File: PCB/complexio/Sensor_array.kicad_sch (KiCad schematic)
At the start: 39 parts, among them J3 Conn_01x12_Pin, Q1 AO3400A, U10 KTIR0711S, U11 KTIR0711S, U12 KTIR0711S, U4 KTIR0711S, U5 KTIR0711S, U6 KTIR0711S, U7 KTIR0711S, U8 KTIR0711S, U9 KTIR0711S

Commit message: Sensor array finished & main schem modified
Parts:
- removed J3: Conn_01x12_Pin, Connector_PinHeader_2.54mm:PinHeader_1x12_P2.54mm_Horizontal, symbol Connector:Conn_01x12_Pin
- added C17, C19, C21, C23, C25, C27, C28, C30, C31: 100n, Capacitor_SMD:C_0402_1005Metric, symbol Device:C
- added C18, C20, C22, C24, C26, C29, C32: 1u, Capacitor_SMD:C_0402_1005Metric, symbol Device:C
- added J1: Conn_01x21_Pin, Connector_PinHeader_1.27mm:PinHeader_1x21_P1.27mm_Horizontal, symbol Connector:Conn_01x21_Pin
- added R23, R24: 47, Resistor_SMD:R_1206_3216Metric, symbol Device:R
- added R25, R26: 47k, Resistor_SMD:R_0402_1005Metric, symbol Device:R
- added R27, R30: 10k, Resistor_SMD:R_0402_1005Metric, symbol Device:R
- added U13, U14, U15, U16, U17, U18, U19: KTIR0711S, KTIR0711S:KTIR0711S, symbol KTIR0711S:KTIR0711S
- added U20: SN74LVC16T245DGGR, SN74LVC16T245DGGR:SN74LVC16T245DGGR, symbol SN74LVC16T245DGGR:SN74LVC16T245DGGR
- R12, R13, R5, R8: footprint Resistor_SMD:R_0402_1005Metric -> Resistor_SMD:R_1206_3216Metric; JLCPCB Part # C11930 -> C702856; MFR.Part # RTT02470JTH -> RCT0647RJLF; Manufacturer RALEC -> HKR(Hong Kong Resistors); Package 0402 -> 1206
- R16: value 47 -> 47k; JLCPCB Part # C11930 -> C22356233; MFR.Part # RTT02470JTH -> RCA0247KJLF; Manufacturer RALEC -> HKR(Hong Kong Resistors)
- R17, R18: value 10k -> 47; footprint Resistor_SMD:R_0402_1005Metric -> Resistor_SMD:R_1206_3216Metric; JLCPCB Part # C174175 -> C702856; MFR.Part # RCT0210KJLF -> RCT0647RJLF; Package 0402 -> 1206
- R19, R20, R21, R22: value 10k -> 47k; JLCPCB Part # C174175 -> C22356233; MFR.Part # RCT0210KJLF -> RCA0247KJLF
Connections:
- net GND: now also C17.2, C18.2, C19.2, C20.2, C21.2, C22.2, C23.2, C24.2, C25.2, C26.2, C27.2, C28.2, C29.2, C30.2, C31.2, C32.2, J1.3 (Pin_3), U13.2 (emitter), U14.2 (emitter), U15.2 (emitter), U16.2 (emitter), U17.2 (emitter), U18.2 (emitter), U19.2 (emitter), U20.1 (1DIR), U20.10 (GND), U20.15 (GND), U20.21 (GND), U20.24 (2DIR), U20.28 (GND), U20.34 (GND), U20.39 (GND), U20.4 (GND), U20.45 (GND); no longer R19.1, R22.1
- net LED_Cathode: now also U14.4 (cathode), U15.4 (cathode), U18.4 (cathode), U19.4 (cathode); no longer U12.4 (cathode)
- net OUT1: now also U20.2 (1B1)
- net OUT2: now also U20.3 (1B2)
- net OUT3: now also U20.5 (1B3); no longer R4.1, U6.3 (collector)
- net OUT4: now also U20.6 (1B4)
- net OUT5: now also R15.1, U12.3 (collector), U20.8 (1B5); no longer R17.2, R18.2
- net OUT6: now also R19.1, U14.3 (collector), U20.9 (1B6); no longer R20.2, R21.2
- net OUT7: now also U20.11 (1B7); no longer R10.1, U10.3 (collector)
- net OUT8: now also R25.1, U18.3 (collector), U20.12 (1B8); no longer R14.1, U11.3 (collector)
- net OUT9: now also R7.1, U8.3 (collector), U20.13 (2B1); no longer R15.1, U12.3 (collector)
- net at U10.1 (anode): now also R13.2; no longer R13.1
- net at U8.1 (anode): now also R8.2; no longer R8.1
- net at U4.1 (anode): now also R5.2; no longer R12.1
- net OUT10: now reaches R9.1, U9.3 (collector)
- net OUT10: now also U20.14 (2B2); no longer R20.1
- net at U6.1 (anode): now also R12.2; no longer R5.1
- net +5V: now reaches R18.1, R19.2
- net +5V: now also C10.1, C11.1, C12.1, C13.1, C14.1, C15.1, C16.1, R10.2, R11.2, R12.1, R13.1, R14.2, R15.2, R16.2, R17.1, R2.2, R20.2, R21.2, R22.2, R3.2, R4.2, R5.1, R6.2, R7.2, R8.1, R9.2, C17.1, C18.1, C19.1, C20.1, C21.1, C22.1, C23.1, C24.1, C25.1, C26.1, C27.1, C28.1, J1.1 (Pin_1), R23.1, R24.1, R25.2, R26.2, U20.18 (VCCB), U20.7 (VCCB)
- net at R21.1: now also U16.3 (collector); no longer R22.2
- net at U12.1 (anode): now also R17.2; no longer R16.1
- net LEDON renamed ledon
- net ledon: now also J1.5 (Pin_5)
- removed net VCC: C10.1, C11.1, C12.1, C13.1, C14.1, C15.1, C16.1, R10.2, R11.2, R12.2, R13.2, R14.2, R15.2, R16.2, R2.2, R3.2, R4.2, R5.2, R6.2, R7.2, R8.2, R9.2
- new net: R22.1, U17.3 (collector)
- new net: R10.1, U10.3 (collector)
- new net: R4.1, U6.3 (collector)
- new net: U16.4 (cathode), U18.1 (anode)
- new net: U12.4 (cathode), U14.1 (anode)
- new net: R23.2, U16.1 (anode)
- new net: U13.4 (cathode), U15.1 (anode)
- new net: U17.4 (cathode), U19.1 (anode)
- new net: R18.2, U13.1 (anode)
- new net: R24.2, U17.1 (anode)
- new net +3V3: C29.1, C30.1, C31.1, C32.1, J1.2 (Pin_2), R27.1, R30.1, U20.31 (VCCA), U20.42 (VCCA)
- new net OUT11: U20.16 (2B3)
- new net OUT12: R14.1, U11.3 (collector), U20.17 (2B4)
- new net OUT13: R16.1, U13.3 (collector), U20.19 (2B5)
- new net OUT14: R20.1, U15.3 (collector), U20.20 (2B6)
- new net OUT15: U20.22 (2B7)
- new net OUT16: R26.1, U19.3 (collector), U20.23 (2B8)
- new net oe: J1.4 (Pin_4), R27.2, R30.2, U20.25 (2OE), U20.48 (1OE)
- new net sen1: J1.6 (Pin_6), U20.47 (1A1)
- new net sen10: J1.15 (Pin_15), U20.35 (2A2)
- new net sen11: J1.16 (Pin_16), U20.33 (2A3)
- new net sen12: J1.17 (Pin_17), U20.32 (2A4)
- new net sen13: J1.18 (Pin_18), U20.30 (2A5)
- new net sen14: J1.19 (Pin_19), U20.29 (2A6)
- new net sen15: J1.20 (Pin_20), U20.27 (2A7)
- new net sen16: J1.21 (Pin_21), U20.26 (2A8)
- new net sen2: J1.7 (Pin_7), U20.46 (1A2)
- new net sen3: J1.8 (Pin_8), U20.44 (1A3)
- new net sen4: J1.9 (Pin_9), U20.43 (1A4)
- new net sen5: J1.10 (Pin_10), U20.41 (1A5)
- new net sen6: J1.11 (Pin_11), U20.40 (1A6)
- new net sen7: J1.12 (Pin_12), U20.38 (1A7)
- new net sen8: J1.13 (Pin_13), U20.37 (1A8)
- new net sen9: J1.14 (Pin_14), U20.36 (2A1)
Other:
- note added: "0.1uF and 1uF caps for every 2 sensors to reduce noise"
- note added: "HOLY TUFF"
- note added: "NOTE: Place 100nF caps close to their respective vcc pins"
- note added: "Sensor array consisting of 16 KTIR0711S sensors"
- note added: "Transceiver to step down +5v coming from the sensors to +3.3v for STM32's ADC pins, which are NOT 5V tolerant(don't even try)"
- note added: "Trasceiver"
- note added: "pair5"
- note added: "pair6"
- note added: "pair7"
- note added: "pair8"
- note added: "sen1-16 gnd 5v 3.3v ledon oe"
- note removed: "0.1uF and 1uF caps for every 3 sensors to reduce noise"
- note removed: "Sensor array consisting of 9 KTIR0711S sensors"
- note removed: "solo"
- moved on the sheet: C10, C11, C12, Q1, R10, R11, R14, R2, R3, R4, R6, R7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

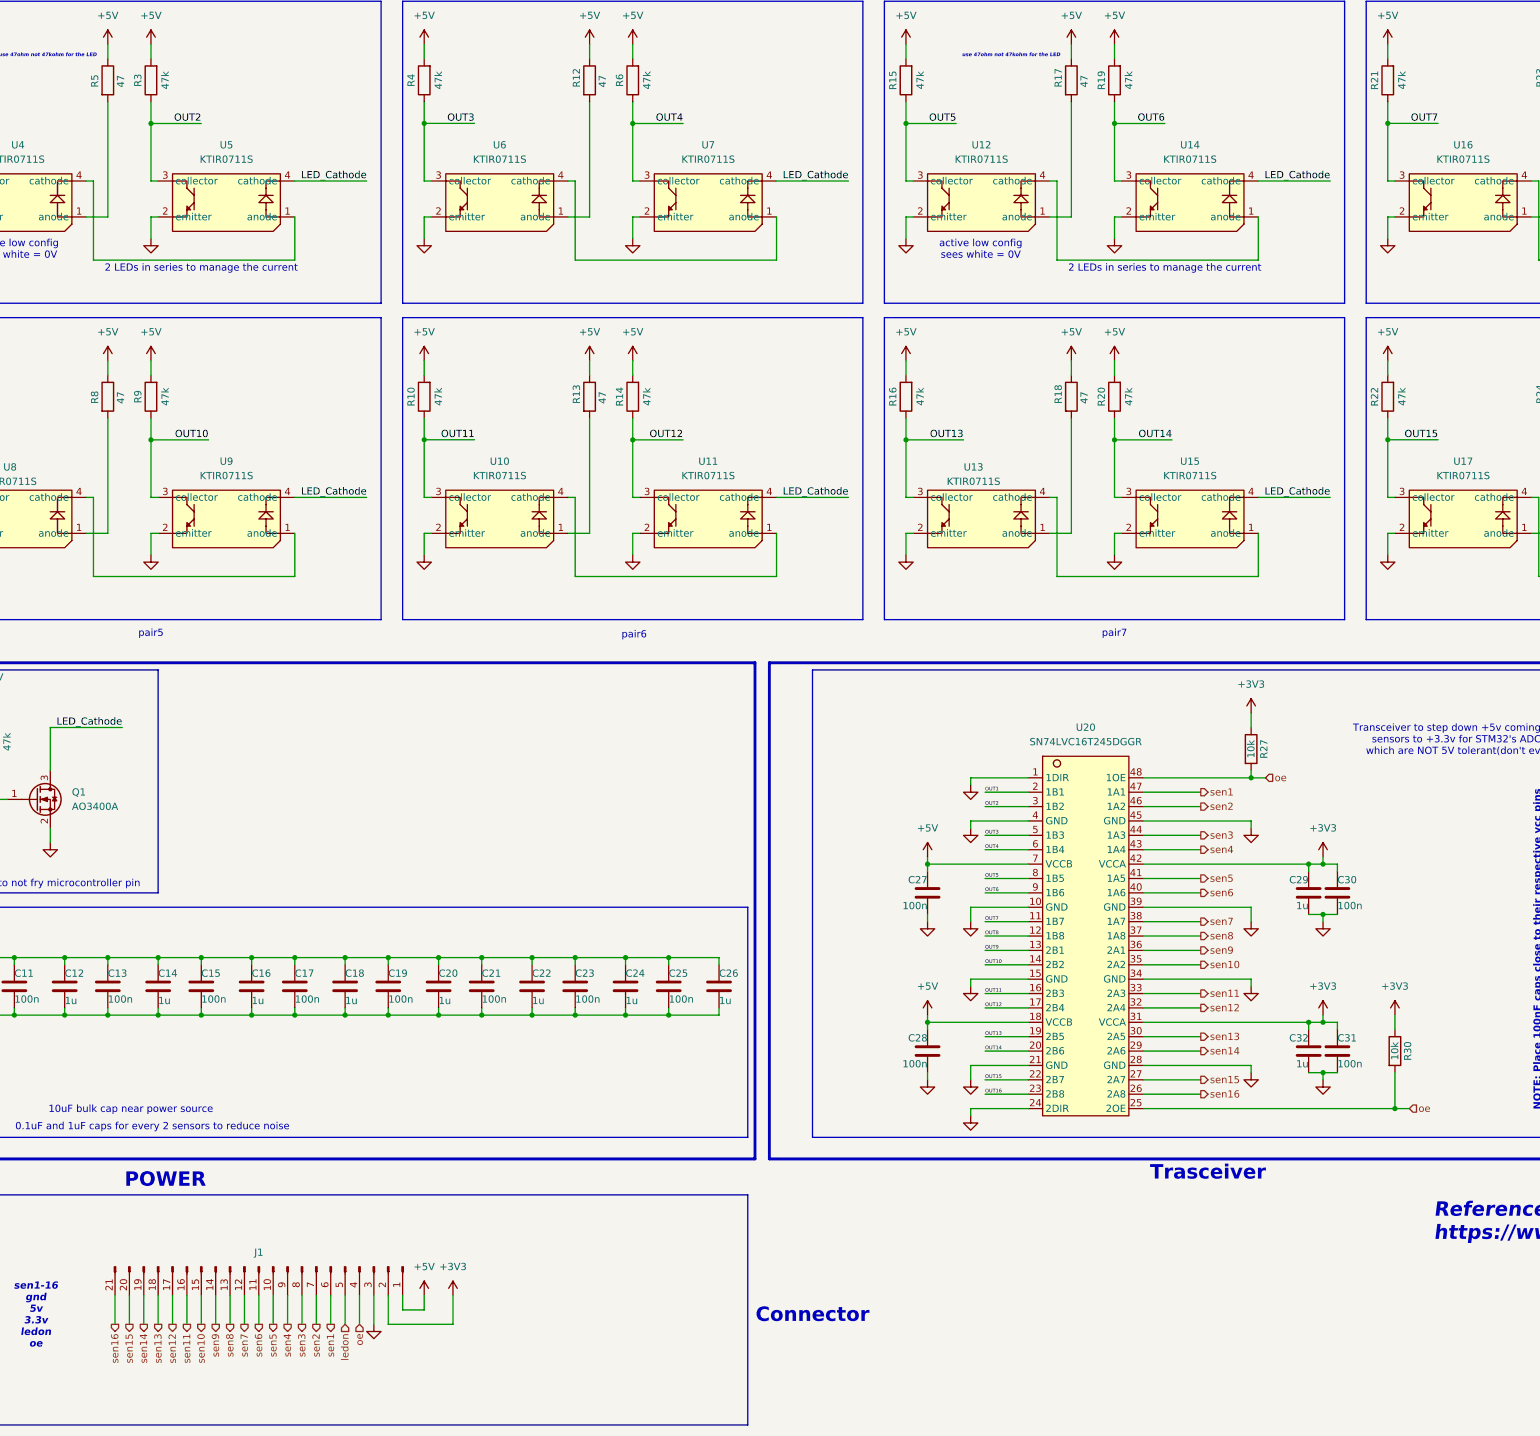
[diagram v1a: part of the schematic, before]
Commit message: Changed firmware & SMD of mpu6050+minor changes
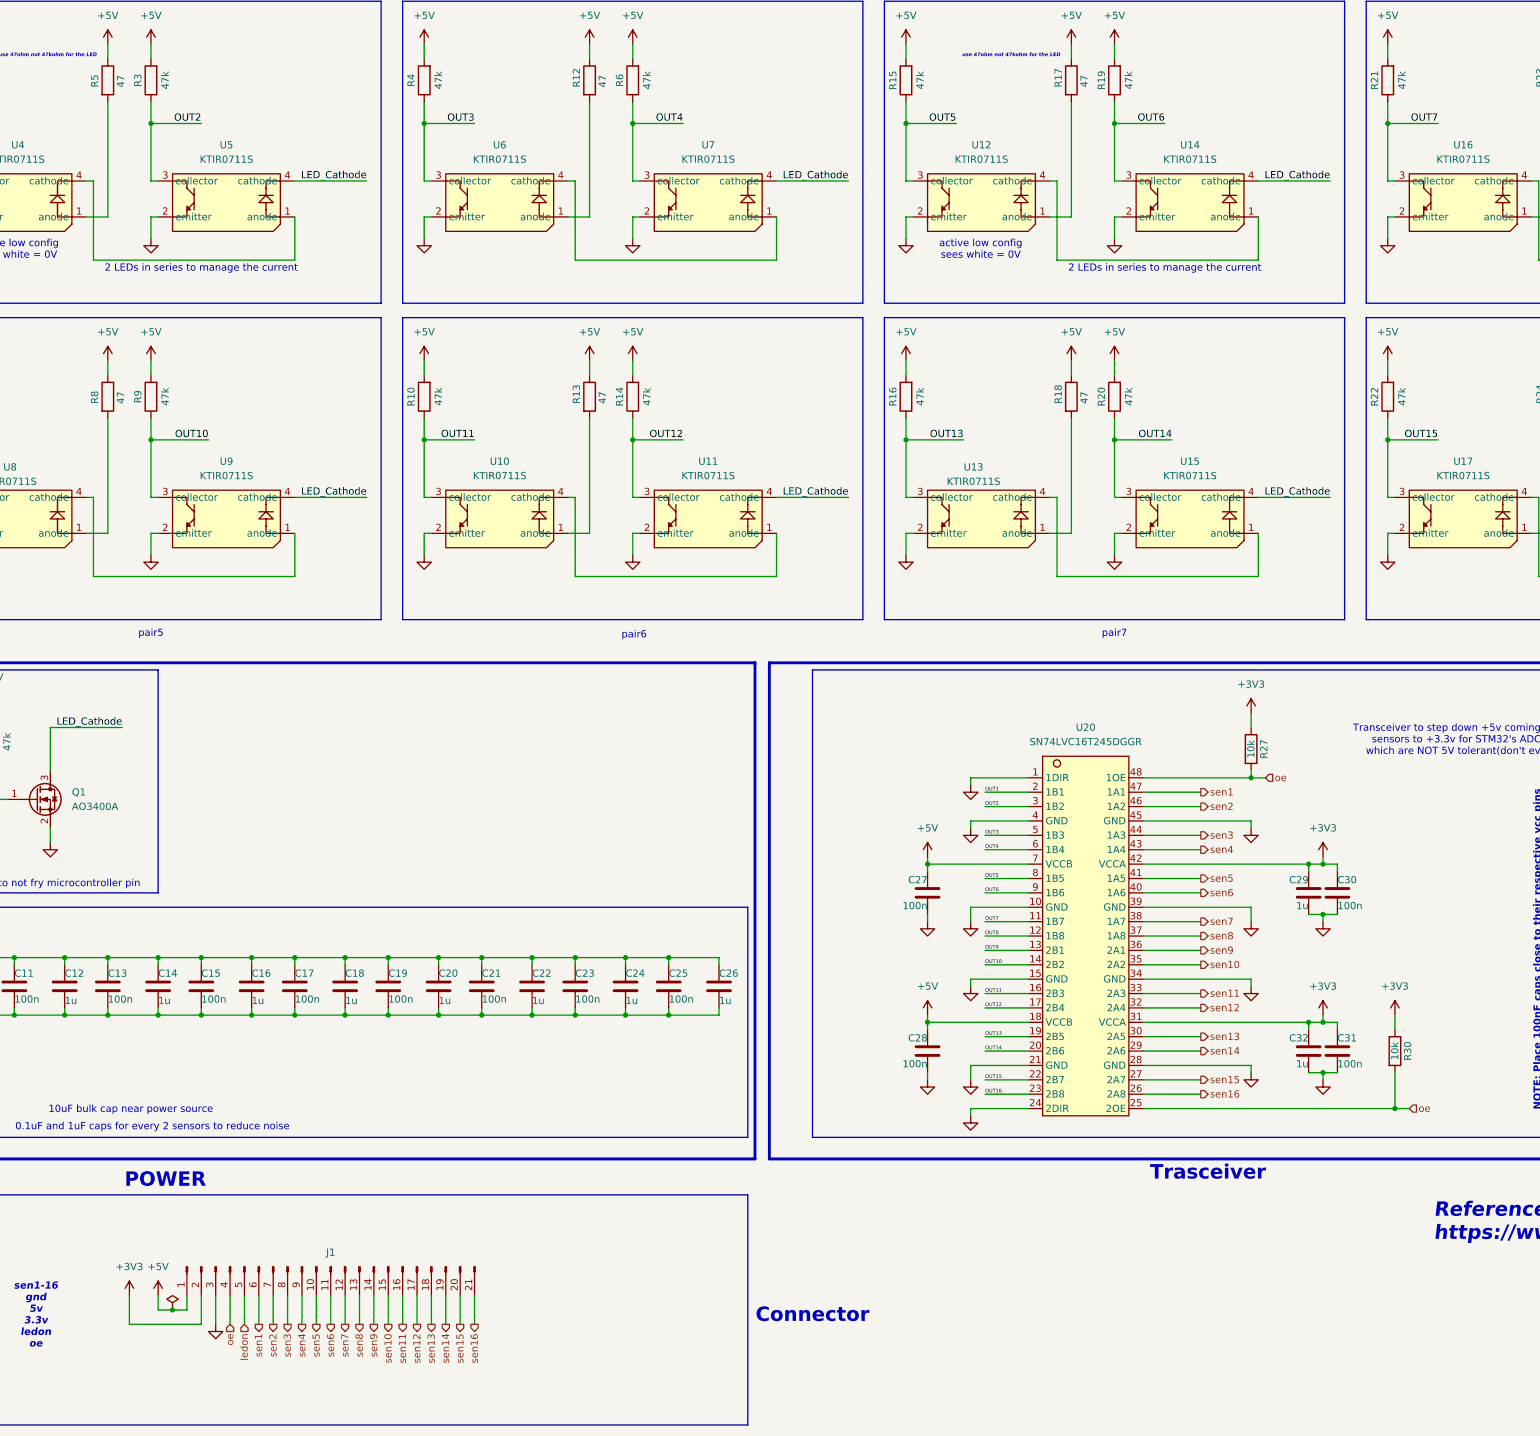
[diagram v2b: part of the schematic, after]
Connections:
- net OUT11: now also R10.1, U10.3 (collector)
- net OUT15: now also R22.1, U17.3 (collector)
- net OUT3: now also R4.1, U6.3 (collector)
- net OUT7: now also R21.1, U16.3 (collector)
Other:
- moved on the sheet: J1
